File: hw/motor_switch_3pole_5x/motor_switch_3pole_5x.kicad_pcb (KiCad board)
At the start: 2 copper layers, 93 x 89.6 mm, 168 parts, among them J1 CONN_2X1, J10 WAGO 233-504, J11 WAGO 233-504, J12 CONN-ISP-6, J13 WAGO 243-723, J14 WAGO 243-724, J15 WAGO 243-721, J16 WAGO 243-722, J17 CONN_1, J18 CONN_1, J19 tp_output_motor_0_up, J2 WAGO 2081-1122, J20 tp_output_motor_on, J21 tp_output_motor_1_up, J22 tp_output_motor_1_on, J23 tp_output_motor_2_up, J24 tp_output_motor_2_on, J25 tp_output_motor_3_up, J26 tp_output_motor_3_on, J27 tp_output_motor_4_up, J28 tp_output_motor_4_on, J29 tp_cseep, J3 WAGO 2081-1122, J30 tp_vcc, J31 tp_gnd, J32 tp_output_button_0_up, J33 tp_output_button_0_down, J34 tp_output_button_1_up, J35 tp_output_button_1_down, J36 tp_output_button_2_up, J37 tp_output_button_2_down, J38 tp_output_button_3_up, J39 tp_output_button_3_down, J4 WAGO 2081-1122, J40 tp_output_button_4_up, J41 tp_output_button_4_down, J42 tp_output_latch, J43 tp_output_data, J44 tp_output_clock, J45 tp_output_reset, J46 tp_miso, J47 tp_txden, J48 tp_txd, J49 tp_rxd, J5 WAGO 2081-1122, J6 WAGO 2081-1122, J7 WAGO 233-504, J8 WAGO 233-504, J9 WAGO 233-504, Q1 BSS138, Q10 BSS138, Q2 BSS138, Q3 BSS138, Q4 BSS138, Q5 BSS138, Q6 BSS138, Q7 BSS138, Q8 BSS138, Q9 BSS138, U1 74HC595, U2 74HC595, U3 25LC256, U4 ATMEGA328-TQFP32, U5 7,3728MHz, U6 MAX487ECSA, U7 AM1S-2405

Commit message: Changed motor_switch_3pole revision from 1 to A Updated §D images Updated gerber files Created BOM and component placement drawings
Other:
- board text added: "motor switch 3pole 5x Rev A"
- board text removed: "motor switch 3pole 5x Rev 1"
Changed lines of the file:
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@@
   (title_block
     (title "motor switch 3pole 5x")
-    (date 2018-09-18)
-    (rev 1)
+    (date 2018-09-26)
+    (rev A)
     (company koewiba)
   )
   (layers
-    (0 F.Cu signal hide)
-    (31 B.Cu signal hide)
+    (0 F.Cu signal)
+    (31 B.Cu signal)
     (32 B.Adhes user)
     (33 F.Adhes user)
@@
       (drillshape 0)
       (scaleselection 1)
-      (outputdirectory "pcb"))
+      (outputdirectory "gerber"))
   )
   (net 0 "")
@@
     (effects (font (size 1 1) (thickness 0.2)) (justify left))
   )
-  (gr_text "motor switch 3pole 5x   Rev 1" (at 168.275 51.435) (layer B.Cu)
+  (gr_text "motor switch 3pole 5x   Rev A" (at 168.275 51.435) (layer B.Cu)
     (effects (font (size 1 1) (thickness 0.2)) (justify right mirror))
   )
-  (gr_text "motor switch 3pole 5x   Rev 1" (at 191.77 51.435) (layer F.Cu)
+  (gr_text "motor switch 3pole 5x   Rev A" (at 191.77 51.435) (layer F.Cu)
     (effects (font (size 1 1) (thickness 0.2)) (justify right))
   )

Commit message: Fixed PCB: Removed copper logo
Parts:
- removed LOGO3: OPEN_HARDWARE_1, Symbol:Symbol_OSHW-Logo_Copper
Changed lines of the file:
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@@
-(kicad_pcb (version 20171130) (host pcbnew 5.0.0-fee4fd1~66~ubuntu16.04.1)
+(kicad_pcb (version 20171130) (host pcbnew 5.0.1-33cea8e~67~ubuntu16.04.1)
   (general
     (thickness 1.6)
@@
     (tracks 921)
     (zones 0)
-    (modules 168)
+    (modules 167)
     (nets 114)
   )
@@
   (title_block
     (title "motor switch 3pole 5x")
-    (date 2018-09-26)
+    (date 2018-10-24)
     (rev A)
     (company koewiba)
@@
     (pad_drill 0.7)
     (pad_to_mask_clearance 0.2)
+    (solder_mask_min_width 0.25)
     (aux_axis_origin 0 0)
     (grid_origin 107.62 129.44)
@@
       (net 81 /bus_atmega328_basic/RXD0))
   )
-  (module Symbol:Symbol_OSHW-Logo_Copper (layer F.Cu)
-    (at 171.729601 117.504541)
-    (descr "Symbol, OSHW-Logo, Copper,")
-    (tags "Symbol, OSHW-Logo, Copper,")
-    (fp_text reference LOGO3 (at 0.09906 -4.38912) (layer F.SilkS) hide
-      (effects (font (size 1 1) (thickness 0.2)))
-    )
-    (fp_text value OPEN_HARDWARE_1 (at 0.30988 6.56082) (layer F.Fab) hide
-      (effects (font (size 1 1) (thickness 0.2)))
-    )
-    (fp_line (start 0.35052 0.89916) (end 0.7493 1.89992) (layer F.Cu) (width 0.381))
-    (fp_line (start -0.35052 0.89916) (end -0.70104 1.89992) (layer F.Cu) (width 0.381))
-    (fp_line (start -0.70104 0.70104) (end -0.35052 0.89916) (layer F.Cu) (width 0.381))
-    (fp_line (start -0.94996 0.39878) (end -0.70104 0.70104) (layer F.Cu) (width 0.381))
-    (fp_line (start -1.00076 -0.09906) (end -0.94996 0.39878) (layer F.Cu) (width 0.381))
-    (fp_line (start -0.8509 -0.55118) (end -1.00076 -0.09906) (layer F.Cu) (width 0.381))
-    (fp_line (start -0.44958 -0.89916) (end -0.8509 -0.55118) (layer F.Cu) (width 0.381))
-    (fp_line (start -0.0508 -1.00076) (end -0.44958 -0.89916) (layer F.Cu) (width 0.381))
-    (fp_line (start 0.39878 -0.94996) (end -0.0508 -1.00076) (layer F.Cu) (width 0.381))
-    (fp_line (start 0.8509 -0.59944) (end 0.39878 -0.94996) (layer F.Cu) (width 0.381))
-    (fp_line (start 1.00076 -0.24892) (end 0.8509 -0.59944) (layer F.Cu) (width 0.381))
-    (fp_line (start 1.00076 0.14986) (end 1.00076 -0.24892) (layer F.Cu) (width 0.381))
-    (fp_line (start 0.8509 0.55118) (end 1.00076 0.14986) (layer F.Cu) (width 0.381))
-    (fp_line (start 0.65024 0.7493) (end 0.8509 0.55118) (layer F.Cu) (width 0.381))
-    (fp_line (start 0.35052 0.89916) (end 0.65024 0.7493) (layer F.Cu) (width 0.381))
-    (fp_line (start -1.9304 0.5207) (end -1.7907 0.91948) (layer F.Cu) (width 0.381))
-    (fp_line (start -2.4892 0.32004) (end -1.9304 0.5207) (layer F.Cu) (width 0.381))
-    (fp_line (start -2.47904 -0.381) (end -2.4892 0.32004) (layer F.Cu) (width 0.381))
-    (fp_line (start -1.9304 -0.48006) (end -2.47904 -0.381) (layer F.Cu) (width 0.381))
-    (fp_line (start -1.76022 -0.96012) (end -1.9304 -0.48006) (layer F.Cu) (width 0.381))
-    (fp_line (start -2.00914 -1.50114) (end -1.76022 -0.96012) (layer F.Cu) (width 0.381))
-    (fp_line (start -1.49098 -2.02946) (end -2.00914 -1.50114) (layer F.Cu) (width 0.381))
-    (fp_line (start -0.9398 -1.76022) (end -1.49098 -2.02946) (layer F.Cu) (width 0.381))
-    (fp_line (start -0.5207 -1.9304) (end -0.9398 -1.76022) (layer F.Cu) (width 0.381))
-    (fp_line (start -0.30988 -2.47904) (end -0.5207 -1.9304) (layer F.Cu) (width 0.381))
-    (fp_line (start 0.381 -2.46126) (end -0.30988 -2.47904) (layer F.Cu) (width 0.381))
-    (fp_line (start 0.55118 -1.92024) (end 0.381 -2.46126) (layer F.Cu) (width 0.381))
-    (fp_line (start 1.02108 -1.71958) (end 0.55118 -1.92024) (layer F.Cu) (width 0.381))
-    (fp_line (start 1.53924 -1.9812) (end 1.02108 -1.71958) (layer F.Cu) (width 0.381))
-    (fp_line (start 2.00914 -1.47066) (end 1.53924 -1.9812) (layer F.Cu) (width 0.381))
-    (fp_line (start 1.7399 -1.00076) (end 2.00914 -1.47066) (layer F.Cu) (width 0.381))
-    (fp_line (start 1.94056 -0.42926) (end 1.7399 -1.00076) (layer F.Cu) (width 0.381))
-    (fp_line (start 2.49936 -0.28956) (end 1.94056 -0.42926) (layer F.Cu) (width 0.381))
-    (fp_line (start 2.49936 0.39116) (end 2.49936 -0.28956) (layer F.Cu) (width 0.381))
-    (fp_line (start 1.88976 0.57912) (end 2.49936 0.39116) (layer F.Cu) (width 0.381))
-    (fp_line (start 1.69926 1.04902) (end 1.88976 0.57912) (layer F.Cu) (width 0.381))
-    (fp_line (start 1.9812 1.52908) (end 1.69926 1.04902) (layer F.Cu) (width 0.381))
-    (fp_line (start 1.50876 2.0193) (end 1.9812 1.52908) (layer F.Cu) (width 0.381))
-    (fp_line (start 1.06934 1.6891) (end 1.50876 2.0193) (layer F.Cu) (width 0.381))
-    (fp_line (start 0.73914 1.8796) (end 1.06934 1.6891) (layer F.Cu) (width 0.381))
-    (fp_line (start -0.98044 1.7399) (end -0.70104 1.89992) (layer F.Cu) (width 0.381))
-    (fp_line (start -1.50114 2.00914) (end -0.98044 1.7399) (layer F.Cu) (width 0.381))
-    (fp_line (start -2.03962 1.49098) (end -1.50114 2.00914) (layer F.Cu) (width 0.381))
-    (fp_line (start -1.78054 0.92964) (end -2.03962 1.49098) (layer F.Cu) (width 0.381))
-    (fp_line (start -2.03962 2.78892) (end -2.4003 2.65938) (layer F.Cu) (width 0.381))
-    (fp_line (start -1.9304 3.07086) (end -2.03962 2.78892) (layer F.Cu) (width 0.381))
-    (fp_line (start -1.8796 3.4798) (end -1.9304 3.07086) (layer F.Cu) (width 0.381))
-    (fp_line (start -1.95072 3.93954) (end -1.8796 3.4798) (layer F.Cu) (width 0.381))
-    (fp_line (start -2.16916 4.11988) (end -1.95072 3.93954) (layer F.Cu) (width 0.381))
-    (fp_line (start -2.47904 4.191) (end -2.16916 4.11988) (layer F.Cu) (width 0.381))
-    (fp_line (start -2.7305 4.06908) (end -2.47904 4.191) (layer F.Cu) (width 0.381))
-    (fp_line (start -2.93116 3.74904) (end -2.7305 4.06908) (layer F.Cu) (width 0.381))
-    (fp_line (start -2.9591 3.40106) (end -2.93116 3.74904) (layer F.Cu) (width 0.381))
-    (fp_line (start -2.8702 2.91084) (end -2.9591 3.40106) (layer F.Cu) (width 0.381))
-    (fp_line (start -2.6289 2.66954) (end -2.8702 2.91084) (layer F.Cu) (width 0.381))
-    (fp_line (start -2.37998 2.64922) (end -2.6289 2.66954) (layer F.Cu) (width 0.381))
-    (fp_line (start -0.9906 4.20878) (end -1.34112 4.09956) (layer F.Cu) (width 0.381))
-    (fp_line (start -0.67056 4.18084) (end -0.9906 4.20878) (layer F.Cu) (width 0.381))
-    (fp_line (start -0.43942 3.95986) (end -0.67056 4.18084) (layer F.Cu) (width 0.381))
-    (fp_line (start -0.48006 3.66014) (end -0.43942 3.95986) (layer F.Cu) (width 0.381))
-    (fp_line (start -0.6604 3.50012) (end -0.48006 3.66014) (layer F.Cu) (width 0.381))
-    (fp_line (start -1.04902 3.37058) (end -0.6604 3.50012) (layer F.Cu) (width 0.381))
-    (fp_line (start -1.29032 3.12928) (end -1.04902 3.37058) (layer F.Cu) (width 0.381))
-    (fp_line (start -1.25984 2.86004) (end -1.29032 3.12928) (layer F.Cu) (width 0.381))
-    (fp_line (start -1.02108 2.65938) (end -1.25984 2.86004) (layer F.Cu) (width 0.381))
-    (fp_line (start -0.70104 2.66954) (end -1.02108 2.65938) (layer F.Cu) (width 0.381))
-    (fp_line (start -0.35052 2.75082) (end -0.70104 2.66954) (layer F.Cu) (width 0.381))
-    (fp_line (start 0.20066 4.21894) (end 0.21082 4.20878) (layer F.Cu) (width 0.381))
-    (fp_line (start 0.20066 2.64922) (end 0.20066 4.21894) (layer F.Cu) (width 0.381))
-    (fp_line (start 1.08966 2.65938) (end 1.08966 4.20116) (layer F.Cu) (width 0.381))
-    (fp_line (start 1.04902 3.38074) (end 1.04902 3.37058) (layer F.Cu) (width 0.381))
-    (fp_line (start 1.03886 3.37058) (end 1.04902 3.38074) (layer F.Cu) (width 0.381))
-    (fp_line (start 0.24892 3.38074) (end 1.03886 3.37058) (layer F.Cu) (width 0.381))
-    (fp_line (start 2.61874 4.17068) (end 2.9591 2.72034) (layer F.Cu) (width 0.381))
-    (fp_line (start 2.30886 3.0988) (end 2.61874 4.17068) (layer F.Cu) (width 0.381))
-    (fp_line (start 2.02946 4.16052) (end 2.30886 3.0988) (layer F.Cu) (width 0.381))
-    (fp_line (start 1.66878 2.68986) (end 2.02946 4.16052) (layer F.Cu) (width 0.381))
-  )
   (gr_text bottom (at 175.895 138.43) (layer B.Cu)

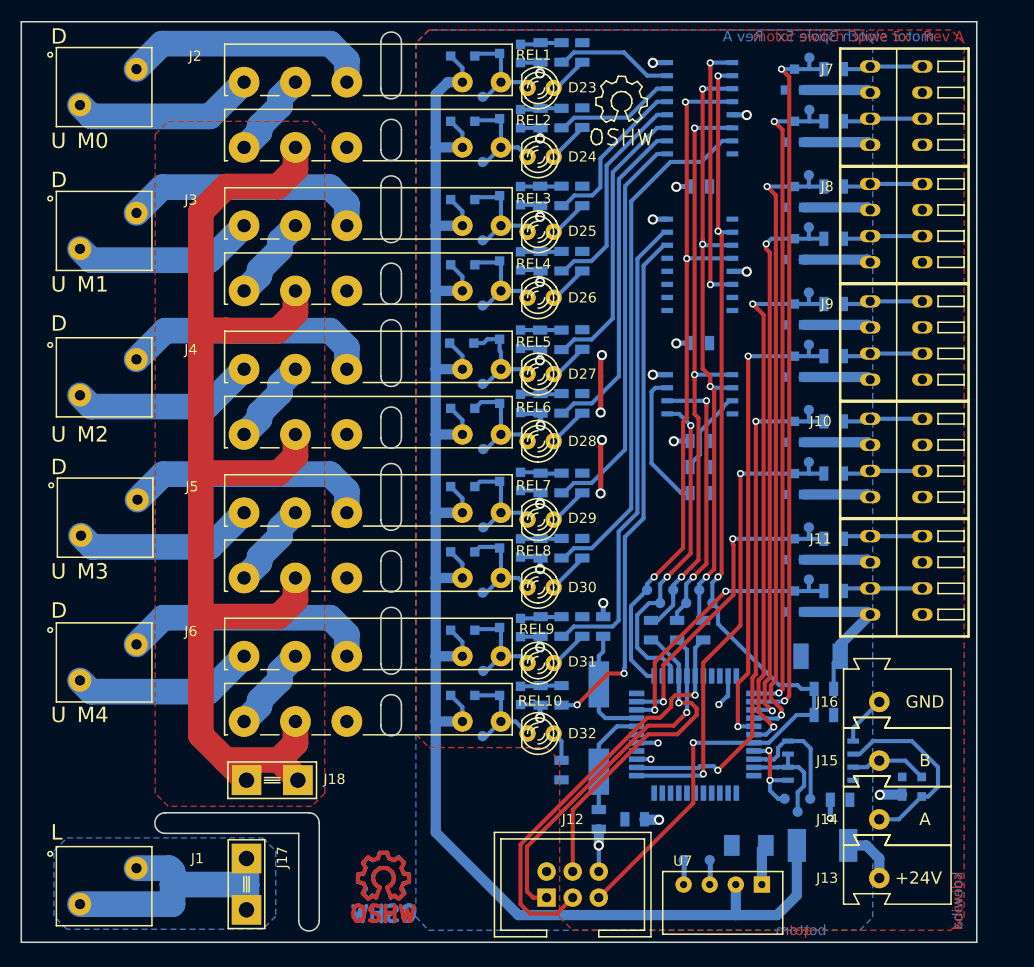
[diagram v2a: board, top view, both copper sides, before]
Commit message: Update to revision B. Fixed footprint of U4
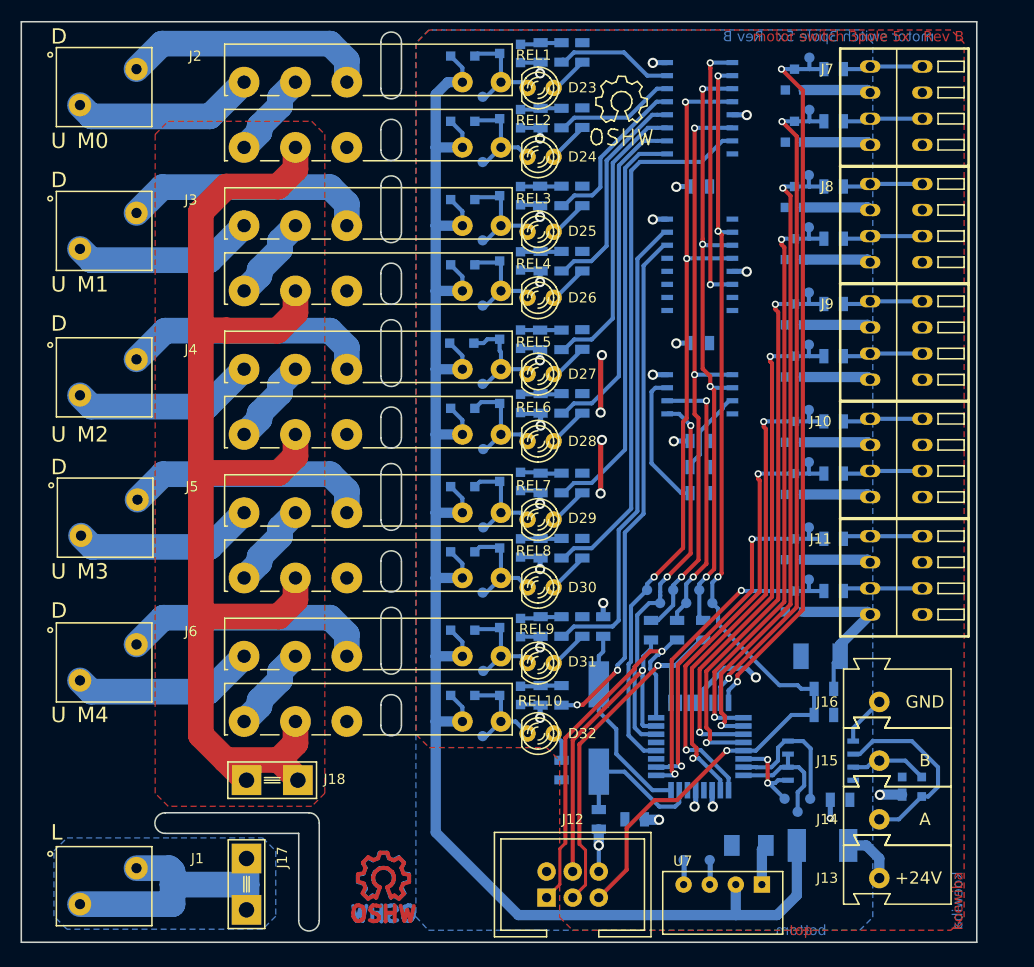
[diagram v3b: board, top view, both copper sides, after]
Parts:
- U4: footprint Housings_QFP:TQFP-44_10x10mm_Pitch0.8mm -> Housings_QFP:TQFP-32_7x7mm_Pitch0.8mm
- moved U4 1.25 mm to (166.0, 120.5), turned to 90 degrees
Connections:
- REL10 pad 3: (no net) -> Net-(REL10-Pad3)
- REL2 pad 3: (no net) -> Net-(REL2-Pad3)
- REL4 pad 3: (no net) -> Net-(REL4-Pad3)
- REL6 pad 3: (no net) -> Net-(REL6-Pad3)
- REL8 pad 3: (no net) -> Net-(REL8-Pad3)
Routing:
- net /output_latch: track 68.9 -> 76.7 mm
- net Net-(C6-Pad1): track 11.5 -> 19.1 mm
- net /bus_atmega328_basic//CSEEP: track 32.1 -> 37.4 mm
- net //button_4_down: track 26.9 -> 31.9 mm
- net //button_4_up: track 31.3 -> 35.9 mm
- net /bus_atmega328_basic/PB5_SCK: track 41.0 -> 36.9 mm
- net GND: track 145.5 -> 149.7 mm
- net /bus_atmega328_basic/PB4_MISO: track 34.9 -> 39.0 mm
- net //button_2_down: track 46.5 -> 50.3 mm
- net //button_3_up: track 51.4 -> 47.7 mm
- net Net-(C5-Pad1): track 10.8 -> 14.3 mm
- net //button_2_up: track 52.7 -> 55.5 mm
- net //button_1_down: track 54.9 -> 57.6 mm
- net //button_3_down: track 46.5 -> 44.0 mm
- net /motor_3_on: track 51.2 -> 53.0 mm
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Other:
- board text added: "motor switch 3pole 5x Rev B"
- board text removed: "motor switch 3pole 5x Rev A"
